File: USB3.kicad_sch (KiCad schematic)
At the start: 10 parts, among them P1 USB_C_Plug, U1 NCP360SNT1G, U2 WE-TVS-82400102

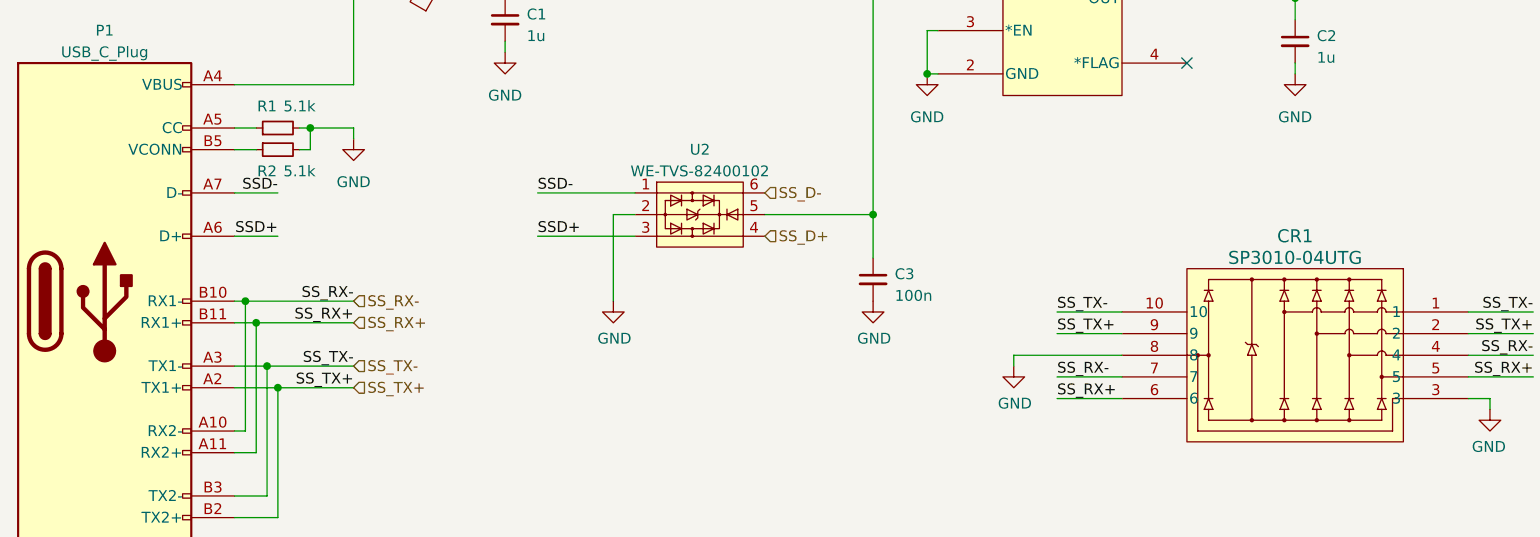
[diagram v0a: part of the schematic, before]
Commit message: update to kicad 9
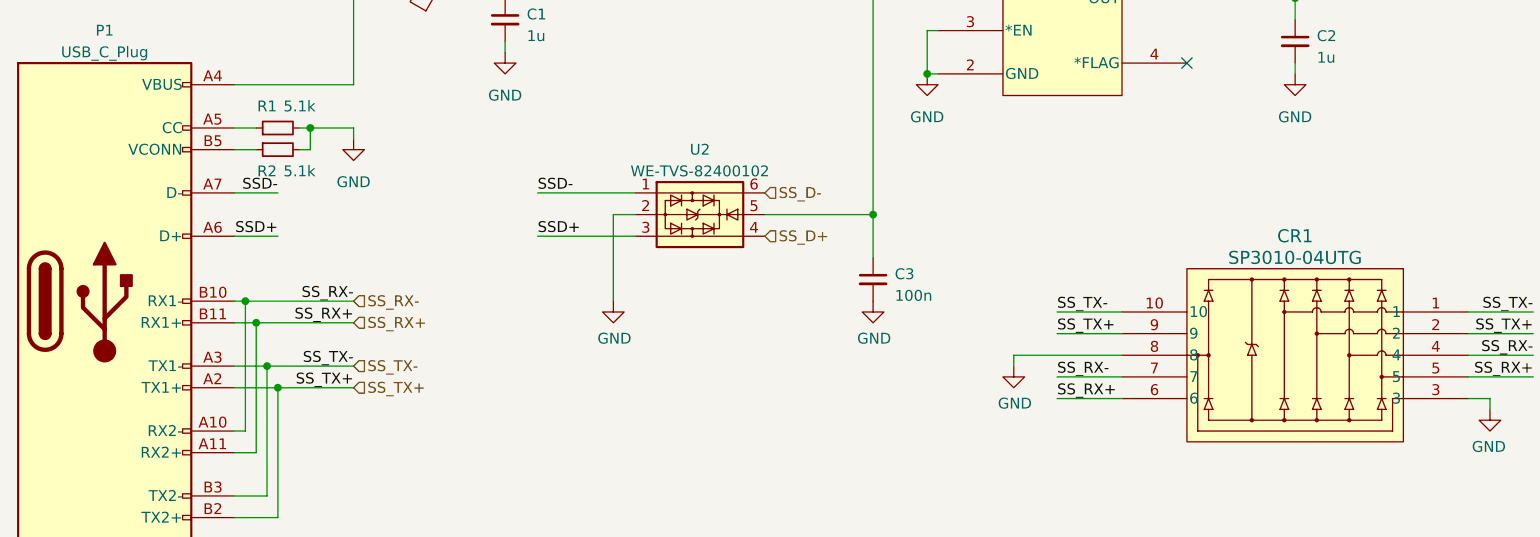
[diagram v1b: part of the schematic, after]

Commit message: begin big refactor
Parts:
- removed P1: USB_C_Plug, Expansion_Card:USB_C_Plug_Molex_105444, symbol Connector:USB_C_Plug
- added P1: USB_C_Receptacle, Snapeda:USB4056-03-A_REVA2_GCT_USB4056-03-A_REVA2, symbol Connector:USB_C_Receptacle
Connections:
- net GND: now also P1.A1 (GND), P1.A12 (GND), P1.B1 (GND), P1.B12 (GND), P1.S1 (SHIELD)
- net SSD+: now also P1.A6 (D+), P1.B6 (D+)
- net SSD-: now also P1.A7 (D-), P1.B7 (D-)
- net SS_RX+: now also CR1.4, CR1.7, P1.A11 (RX2+), P1.B11 (RX1+); no longer CR1.5, CR1.6
- net SS_RX-: now also CR1.5, CR1.6, P1.A10 (RX2-), P1.B10 (RX1-); no longer CR1.4, CR1.7
- net SS_TX+: now also P1.A2 (TX1+), P1.B2 (TX2+)
- net SS_TX-: now also P1.A3 (TX1-), P1.B3 (TX2-)
- net at FB1.1: now also P1.A4 (VBUS), P1.A9 (VBUS), P1.B4 (VBUS), P1.B9 (VBUS)
- net at R1.1: now also P1.A5 (CC1)
- net at R2.1: now also P1.B5 (CC2)

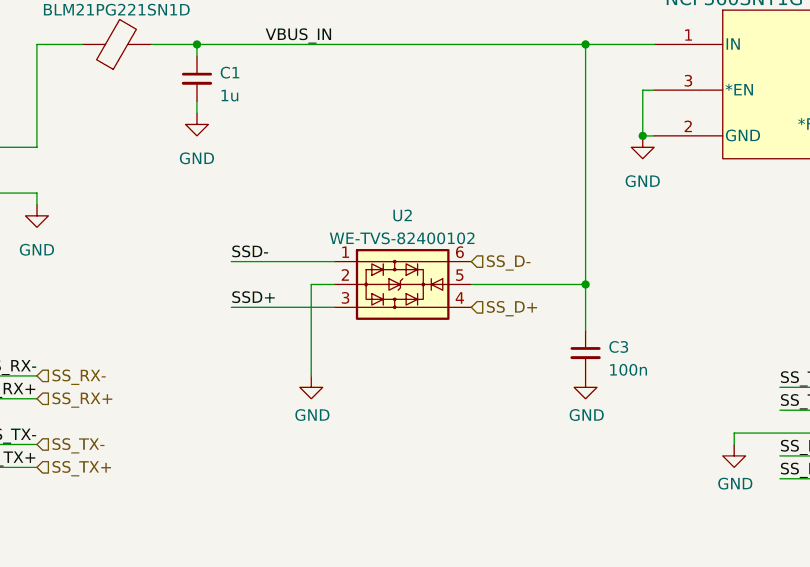
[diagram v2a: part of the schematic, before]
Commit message: more routing, add differential pair netclass
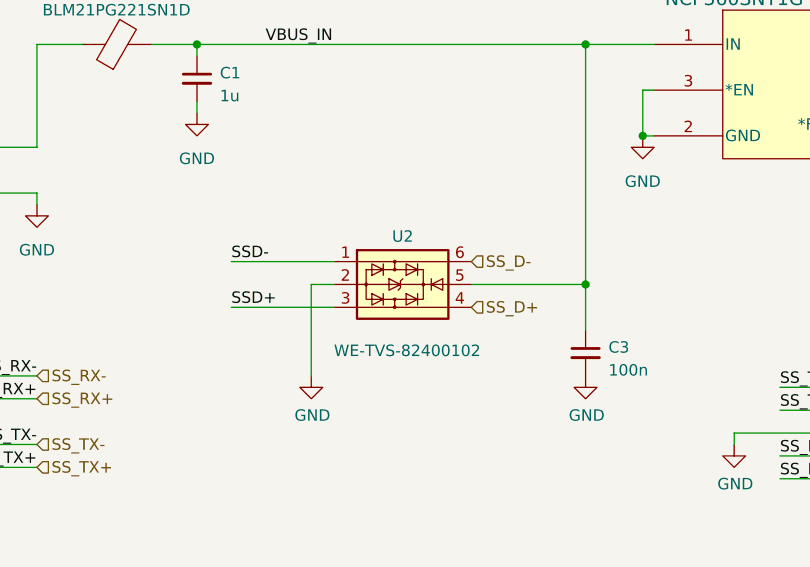
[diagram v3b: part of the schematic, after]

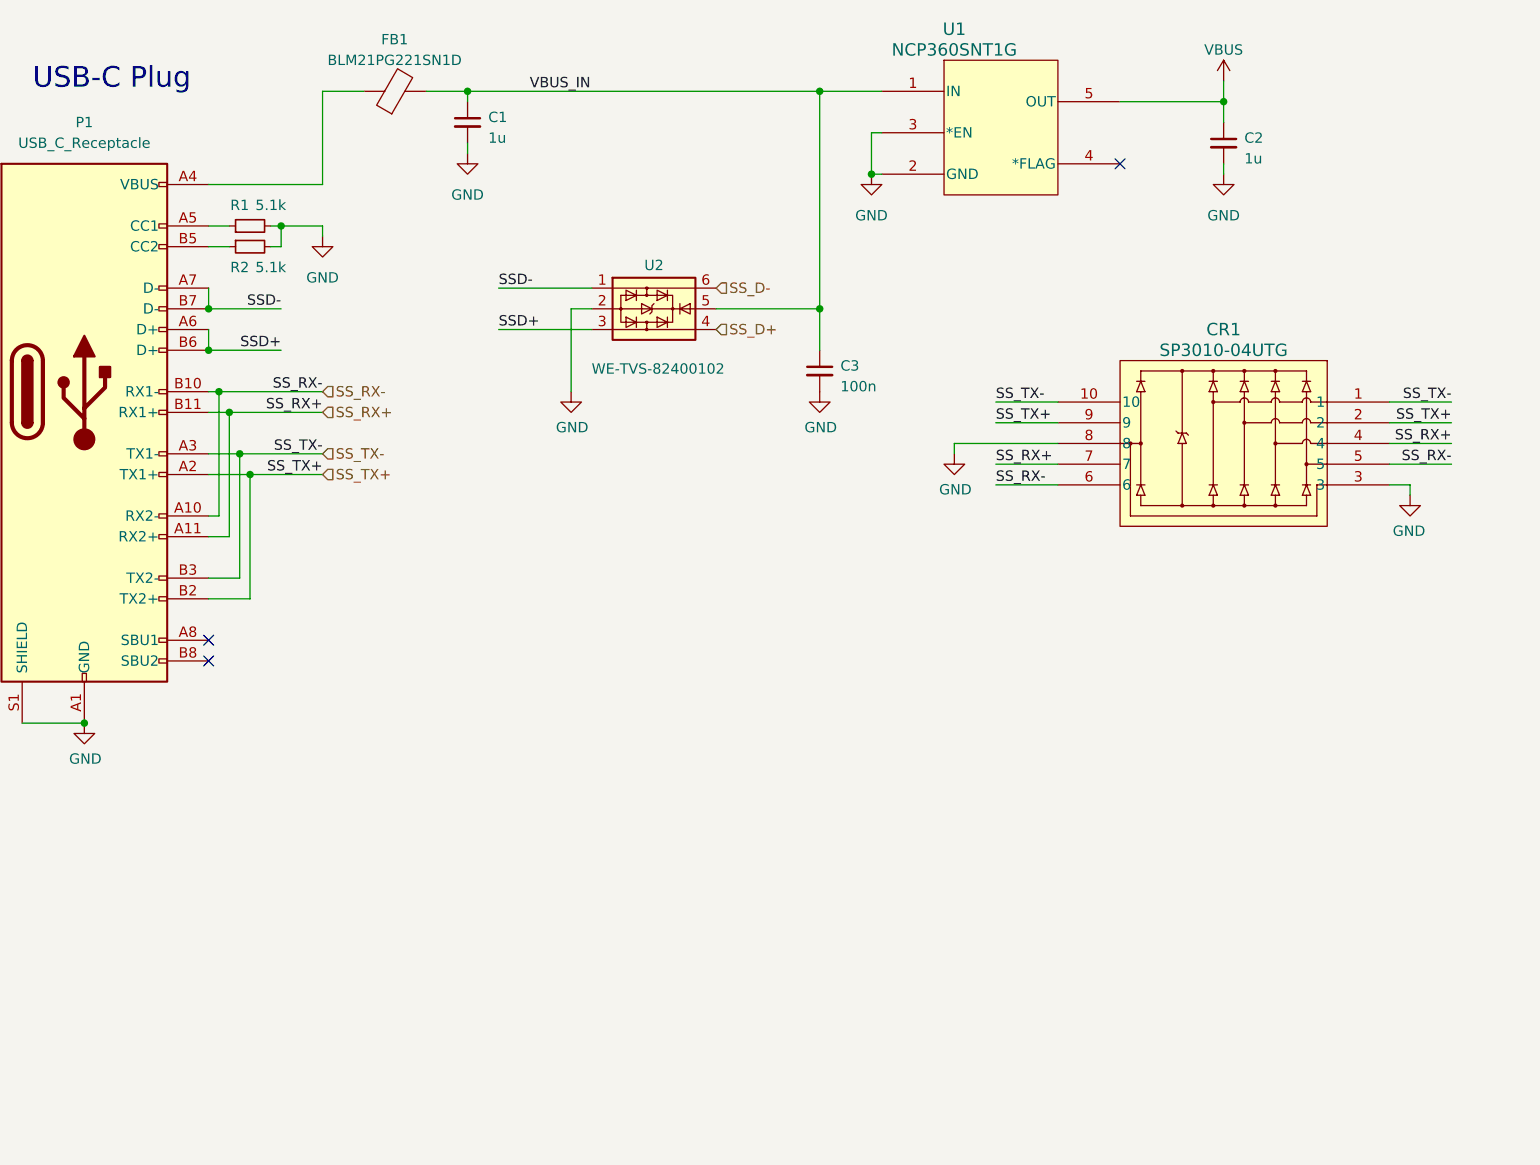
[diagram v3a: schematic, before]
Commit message: begin USB3 layouting ...
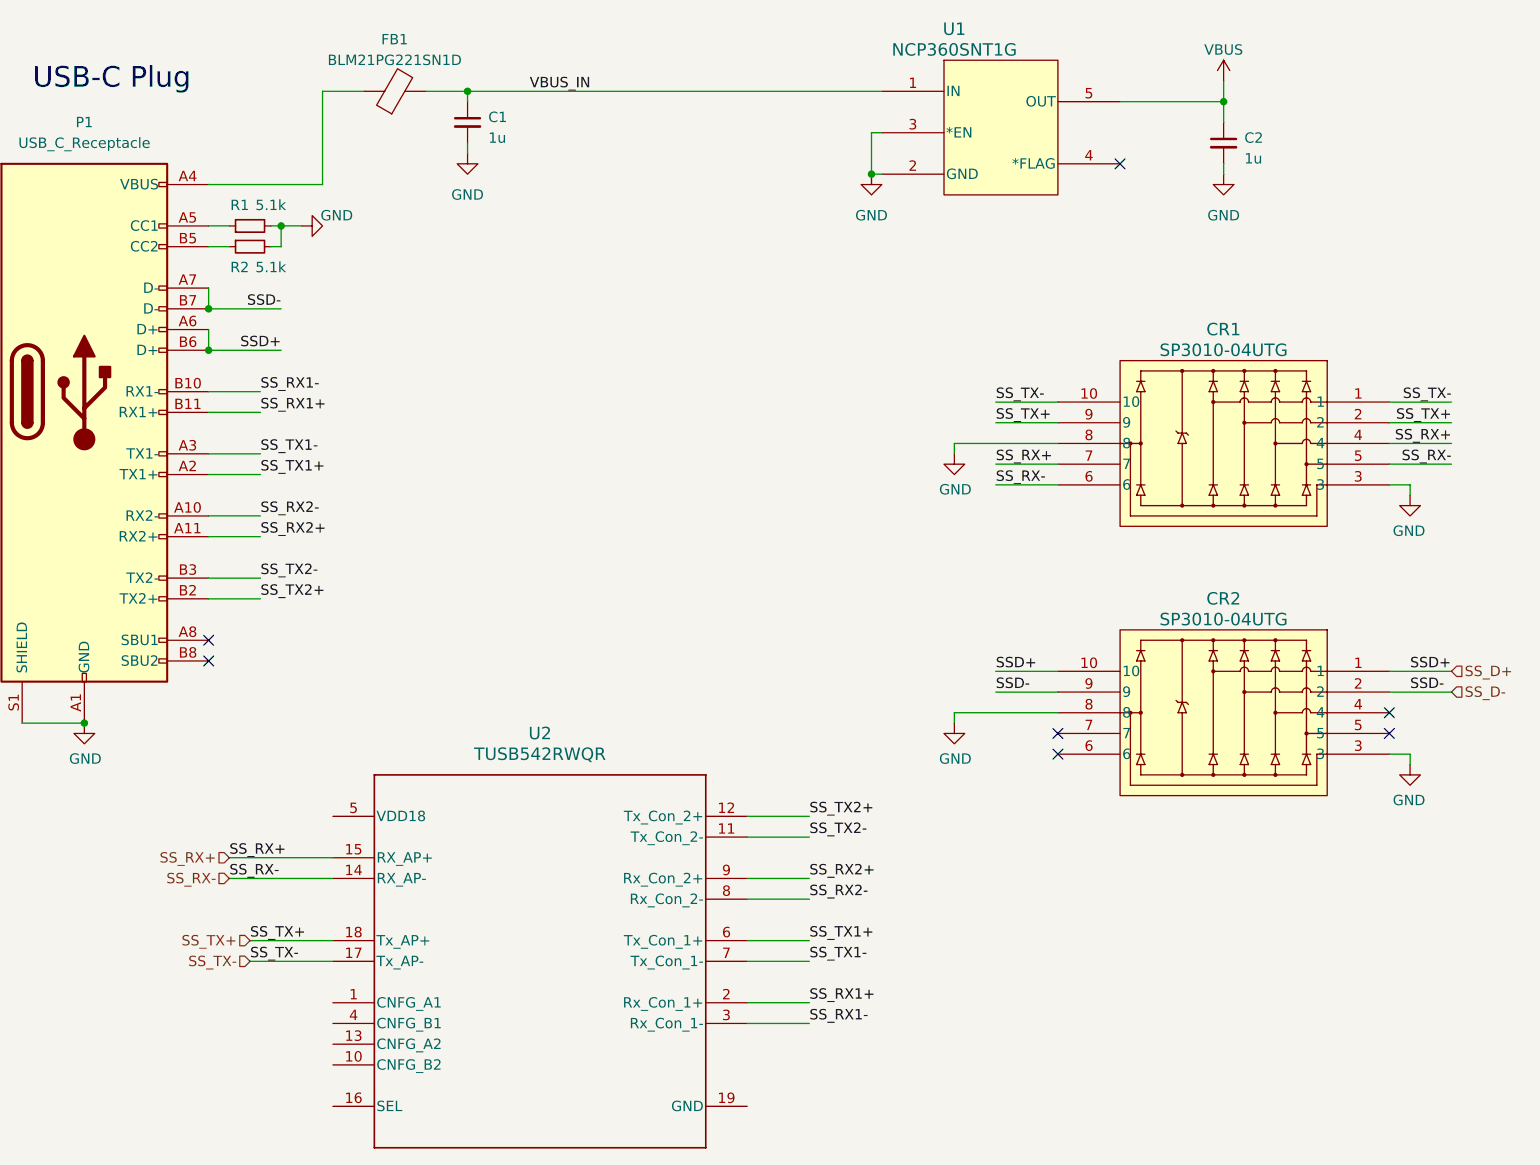
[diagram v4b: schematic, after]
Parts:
- removed C3: 100n, Capacitor_SMD:C_0402_1005Metric, symbol Device:C_Small
- removed U2: WE-TVS-82400102, Package_TO_SOT_SMD:SOT-23-6, symbol Power_Protection:WE-TVS-82400102
- added CR2: SP3010-04UTG, SP3010:UDFEN-10_MO229_LTF, symbol SP3010-04UTG:SP3010-04UTG
- added U2: TUSB542RWQR, Snapeda:RWQ0018A, symbol Snapeda:TUSB542RWQR
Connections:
- net SSD+ is gone; now on net SS_D+: P1.A6 (D+), P1.B6 (D+)
- net SSD- is gone; now on net SS_D-: P1.A7 (D-), P1.B7 (D-)
- net GND: now also CR2.3, CR2.8
- net SS_D+: now also CR2.1, CR2.10
- net SS_D-: now also CR2.2, CR2.9
- net SS_RX+: now also U2.15 (RX_AP+); no longer P1.A11 (RX2+), P1.B11 (RX1+)
- net SS_RX-: now also U2.14 (RX_AP-); no longer P1.A10 (RX2-), P1.B10 (RX1-)
- net SS_TX+: now also U2.18 (Tx_AP+); no longer P1.A2 (TX1+), P1.B2 (TX2+)
- net SS_TX-: now also U2.17 (Tx_AP-); no longer P1.A3 (TX1-), P1.B3 (TX2-)
- new net SS_RX1+: P1.B11 (RX1+), U2.2 (Rx_Con_1+)
- new net SS_RX1-: P1.B10 (RX1-), U2.3 (Rx_Con_1-)
- new net SS_RX2+: P1.A11 (RX2+), U2.9 (Rx_Con_2+)
- new net SS_RX2-: P1.A10 (RX2-), U2.8 (Rx_Con_2-)
- new net SS_TX1+: P1.A2 (TX1+), U2.6 (Tx_Con_1+)
- new net SS_TX1-: P1.A3 (TX1-), U2.7 (Tx_Con_1-)
- new net SS_TX2+: P1.B2 (TX2+), U2.12 (Tx_Con_2+)
- new net SS_TX2-: P1.B3 (TX2-), U2.11 (Tx_Con_2-)
- no-connect marks 3 -> 7

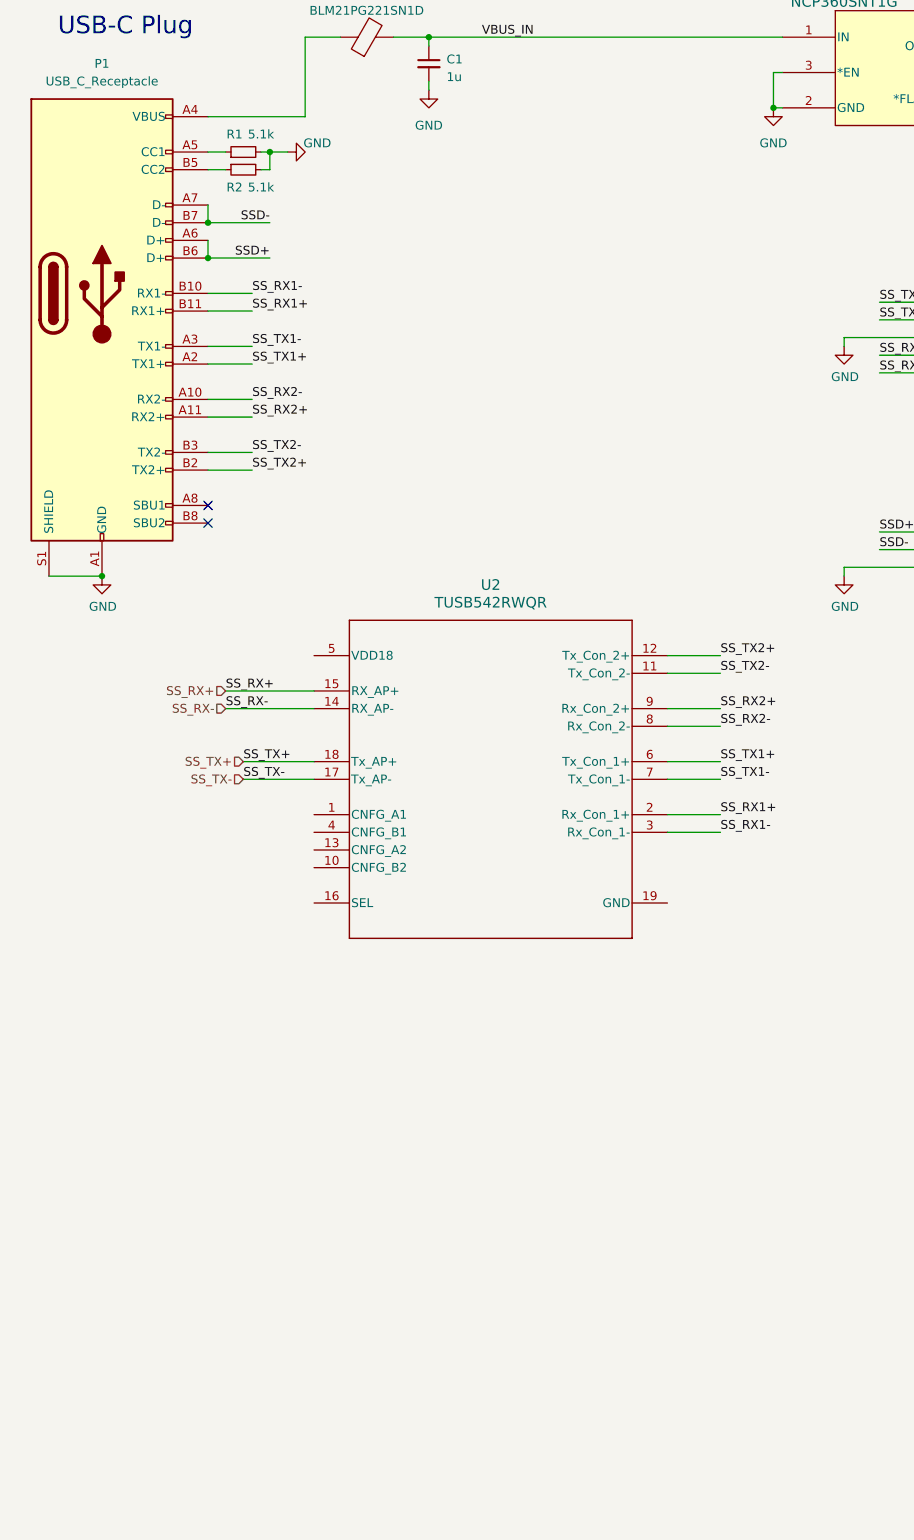
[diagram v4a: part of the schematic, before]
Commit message: add usb3 redriver
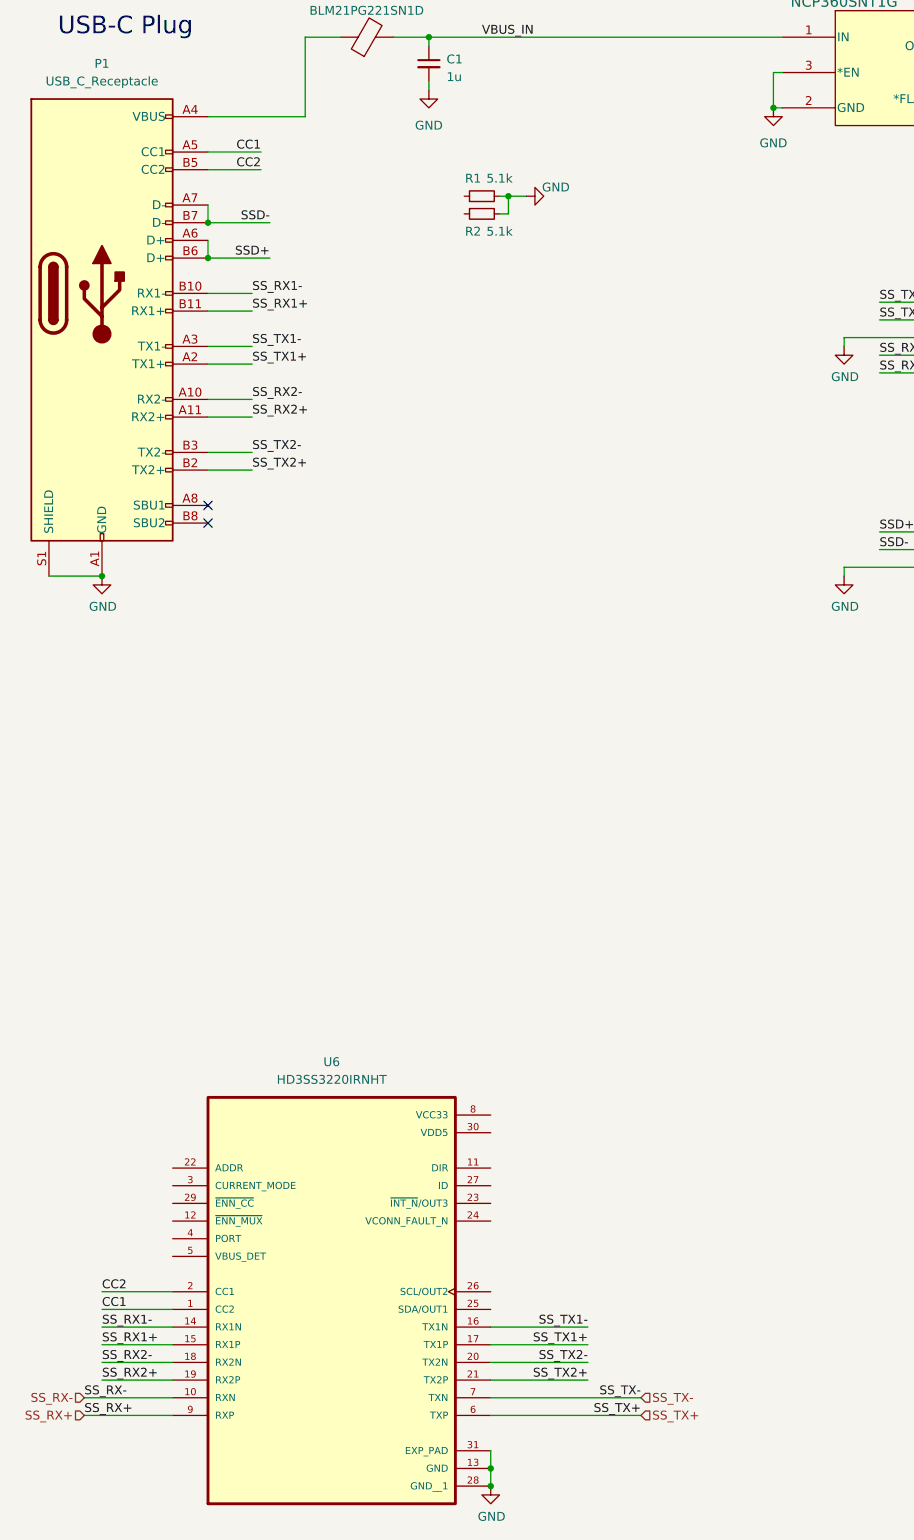
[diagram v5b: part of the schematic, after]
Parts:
- removed U2: TUSB542RWQR, Snapeda:RWQ0018A, symbol Snapeda:TUSB542RWQR
- added U6: HD3SS3220IRNHT, Snapeda:HD3SS3220IRNHT_QFN40P450X250X80-31N120X320, symbol Snapeda:HD3SS3220IRNHT
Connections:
- net GND: now also U6.13 (GND), U6.28 (GND__1), U6.31 (EXP_PAD)
- net SS_RX+: now also U6.9 (RXP)
- net SS_RX-: now also U6.10 (RXN)
- net SS_RX1+: now also U6.15 (RX1P)
- net SS_RX1-: now also U6.14 (RX1N)
- net SS_RX2+: now also U6.19 (RX2P)
- net SS_RX2-: now also U6.18 (RX2N)
- net SS_TX+: now also U6.6 (TXP)
- net SS_TX-: now also U6.7 (TXN)
- net SS_TX1+: now also U6.17 (TX1P)
- net SS_TX1-: now also U6.16 (TX1N)
- net SS_TX2+: now also U6.21 (TX2P)
- net SS_TX2-: now also U6.20 (TX2N)
- net at R1.1: no longer P1.A5 (CC1)
- net at R2.1: no longer P1.B5 (CC2)
- new net CC1: P1.A5 (CC1), U6.1 (CC2)
- new net CC2: P1.B5 (CC2), U6.2 (CC1)
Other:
- moved on the sheet: R1, R2
